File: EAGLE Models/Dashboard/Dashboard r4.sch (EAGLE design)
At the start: 123 parts, among them IC1 AT90CAN128, IC2 MCP2551SO8, IC3 NUP2105L, IC5 FT232RL, Q1 56P2859, U1 74LCX125M

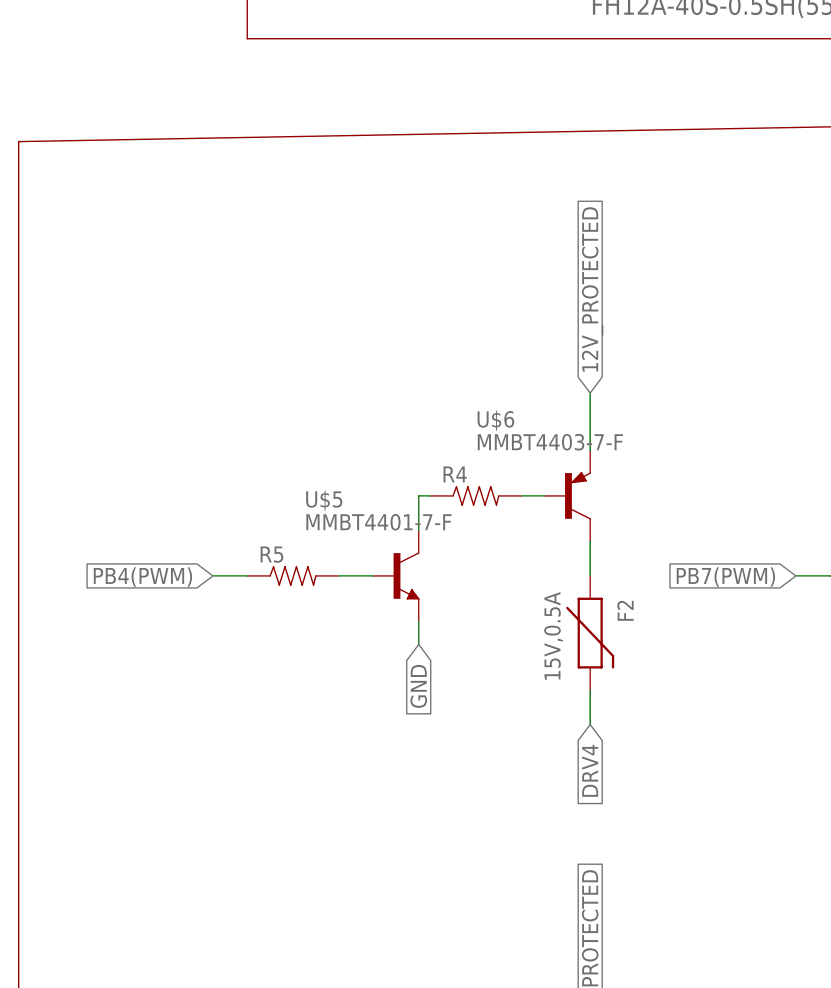
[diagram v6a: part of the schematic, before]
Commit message: moved traces out from under graphics chip, moved reset pin. cleaned up traces
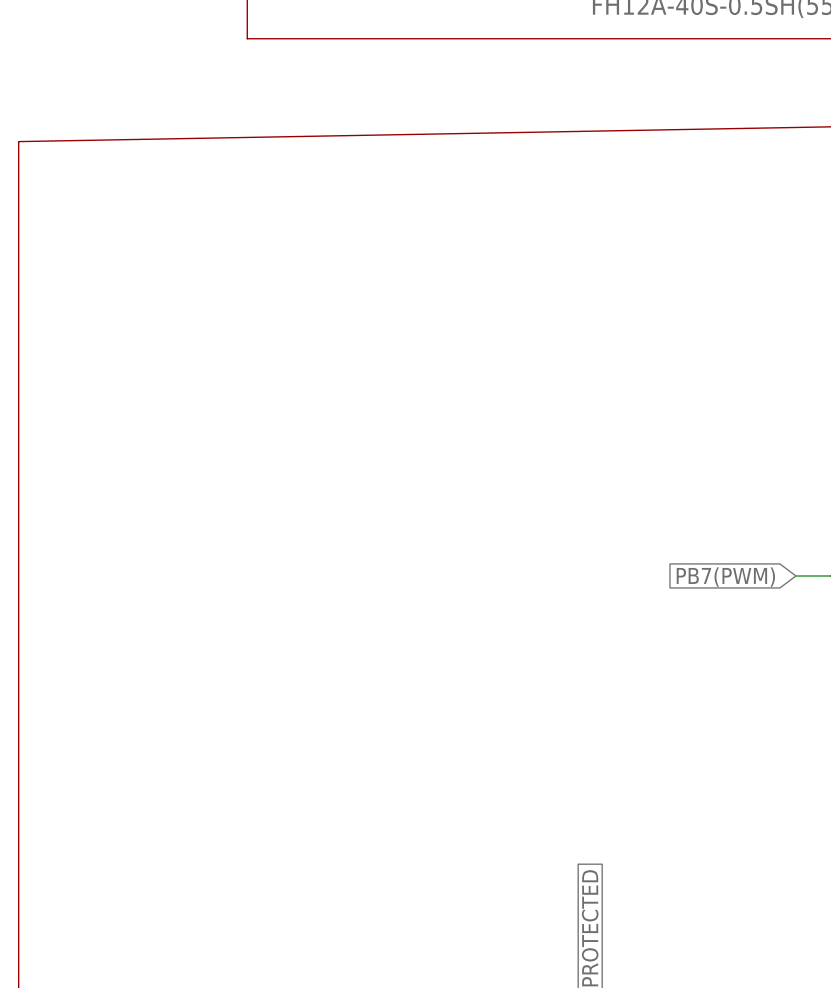
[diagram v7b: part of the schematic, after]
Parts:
- removed F2: 15V,0.5A, SparkFun:PTCSMD
- removed R4, R5: (no value), SparkFun-Resistors:RESISTOR0603
- removed U$5: MMBT4401-7-F, formula electric:MMBT4401-7-F
- removed U$6: MMBT4403-7-F, formula electric:MMBT4403-7-F
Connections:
- removed net DRV4: F2.2
- removed net N$23: R5.2, U$5.B
- removed net N$24: R4.2, U$6.B
- removed net N$25: R4.1, U$5.C
- removed net N$26: F2.1, U$6.C
- net 12V_PROTECTED: no longer U$6.E
- net GND: no longer U$5.E
- net PB4(PWM): no longer R5.1
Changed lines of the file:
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@@
 <?xml version="1.0" encoding="utf-8"?>
 <!DOCTYPE eagle SYSTEM "eagle.dtd">
-<eagle version="8.4.0">
+<eagle version="8.3.2">
 <drawing>
 <settings>
@@
 <part name="C13" library="SparkFun-Capacitors" deviceset="CAP" device="0603-CAP" value="1uF"/>
 <part name="C14" library="SparkFun-Capacitors" deviceset="CAP" device="0603-CAP" value="1uF"/>
-<part name="U$5" library="formula electric" deviceset="MMBT4401-7-F" device=""/>
-<part name="U$6" library="formula electric" deviceset="MMBT4403-7-F" device=""/>
-<part name="R4" library="SparkFun-Resistors" deviceset="RESISTOR" device="0603"/>
-<part name="R5" library="SparkFun-Resistors" deviceset="RESISTOR" device="0603"/>
-<part name="F2" library="SparkFun" deviceset="PTC" device="SMD" value="15V,0.5A"/>
 <part name="U$7" library="formula electric" deviceset="MMBT4401-7-F" device=""/>
 <part name="U$8" library="formula electric" deviceset="MMBT4403-7-F" device=""/>
@@
 <instance part="C13" gate="G$1" x="-231.14" y="31.75"/>
 <instance part="C14" gate="G$1" x="-193.04" y="31.75"/>
-<instance part="U$5" gate="G$1" x="-516.89" y="115.57"/>
-<instance part="U$6" gate="G$1" x="-497.84" y="124.46"/>
-<instance part="R4" gate="G$1" x="-508" y="124.46"/>
-<instance part="R5" gate="G$1" x="-528.32" y="115.57"/>
-<instance part="F2" gate="G$1" x="-495.3" y="110.49" rot="R270"/>
 <instance part="U$7" gate="G$1" x="-516.89" y="41.91"/>
 <instance part="U$8" gate="G$1" x="-497.84" y="50.8"/>
@@
 </segment>
 <segment>
-<pinref part="U$5" gate="G$1" pin="E"/>
-<wire x1="-514.35" y1="110.49" x2="-514.35" y2="107.95" width="0.1524" layer="91"/>
-<label x="-514.35" y="107.95" size="1.778" layer="95" rot="R270" xref="yes"/>
-</segment>
-<segment>
 <pinref part="U$7" gate="G$1" pin="E"/>
 <wire x1="-514.35" y1="36.83" x2="-514.35" y2="34.29" width="0.1524" layer="91"/>
@@
 <pinref part="IC1" gate="G$1" pin="(OC2A)PB4"/>
 </segment>
-<segment>
-<pinref part="R5" gate="G$1" pin="1"/>
-<wire x1="-533.4" y1="115.57" x2="-537.21" y2="115.57" width="0.1524" layer="91"/>
-<label x="-537.21" y="115.57" size="1.778" layer="95" rot="R180" xref="yes"/>
-</segment>
 </net>
 <net name="AVR_MISO" class="0">
@@
 </net>
 <net name="12V_PROTECTED" class="3">
-<segment>
-<pinref part="U$6" gate="G$1" pin="E"/>
-<wire x1="-495.3" y1="129.54" x2="-495.3" y2="135.89" width="0.1524" layer="91"/>
-<label x="-495.3" y="135.89" size="1.778" layer="95" rot="R90" xref="yes"/>
-</segment>
 <segment>
 <pinref part="U$8" gate="G$1" pin="E"/>
@@
 </segment>
 </net>
-<net name="N$23" class="3">
-<segment>
-<pinref part="R5" gate="G$1" pin="2"/>
-<pinref part="U$5" gate="G$1" pin="B"/>
-<wire x1="-523.24" y1="115.57" x2="-519.43" y2="115.57" width="0.1524" layer="91"/>
-</segment>
-</net>
-<net name="N$24" class="3">
-<segment>
-<pinref part="R4" gate="G$1" pin="2"/>
-<pinref part="U$6" gate="G$1" pin="B"/>
-<wire x1="-502.92" y1="124.46" x2="-500.38" y2="124.46" width="0.1524" layer="91"/>
-</segment>
-</net>
-<net name="N$25" class="0">
-<segment>
-<pinref part="R4" gate="G$1" pin="1"/>
-<pinref part="U$5" gate="G$1" pin="C"/>
-<wire x1="-513.08" y1="124.46" x2="-514.35" y2="124.46" width="0.1524" layer="91"/>
-<wire x1="-514.35" y1="124.46" x2="-514.35" y2="120.65" width="0.1524" layer="91"/>
-</segment>
-</net>
-<net name="N$26" class="3">
-<segment>
-<pinref part="F2" gate="G$1" pin="1"/>
-<pinref part="U$6" gate="G$1" pin="C"/>
-<wire x1="-495.3" y1="115.57" x2="-495.3" y2="119.38" width="0.1524" layer="91"/>
-</segment>
-</net>
 <net name="DRV1" class="3">
 <segment>
@@
 </segment>
 </net>
-<net name="DRV4" class="3">
-<segment>
-<pinref part="F2" gate="G$1" pin="2"/>
-<wire x1="-495.3" y1="102.87" x2="-495.3" y2="99.06" width="0.1524" layer="91"/>
-<label x="-495.3" y="99.06" size="1.778" layer="95" rot="R270" xref="yes"/>
-</segment>
-</net>
